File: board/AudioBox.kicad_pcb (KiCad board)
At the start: 2 copper layers, 81.6 x 85 mm, 92 parts, among them J1 Conn_01x04_Male, J2 Conn_Coaxial_Power, J3 AudioJack3_SwitchT, J4 Conn_02x20_Odd_Even, U1 AD1938, U10 LDLN030, U2 TS912, U3 TS912, U4 TS912, U5 TS912, Y1 12.288 MHz

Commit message: half placement done
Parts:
- removed J1: Conn_01x04_Male, Connector_PinHeader_2.54mm:PinHeader_1x04_P2.54mm_Vertical
- removed J2: Conn_Coaxial_Power, Connector_BarrelJack:BarrelJack_Wuerth_6941xx301002
- removed R7: 100K, Resistor_SMD:R_0603_1608Metric_Pad1.05x0.95mm_HandSolder
- C1, C10, C2, C28, C3, C30, C31, C32, C34, C35, C36, C37, C39, C4, C40, C5, C6, C7, C8, C9, R19, R20, R22, R23, R24, R25, R28, R29, R32, R33, U5: moved to B.Cu
- C12: value 10u -> 22u
- IN1, IN2, OUT1, OUT2: value 4833.222_SCH -> 4833.222
- R3: value 4.7K -> 2.2K
- moved C35 77.0 mm to (140.1, 65.7)
- moved U5 73.8 mm to (141.1, 62.4)
- moved C36 73.2 mm to (140.8, 65.1)
- moved C34 70.0 mm to (141.4, 73.5)
- moved R23 66.4 mm to (142.6, 63.5)
- moved IN2 61.2 mm to (102.7, 102.0)
- moved R25 59.4 mm to (143.0, 68.5)
- moved C37 58.6 mm to (140.7, 69.8)
- moved R22 53.4 mm to (140.2, 72.6)
- moved U10 51.4 mm to (96.7, 34.0), turned to 270 degrees
- moved R24 50.6 mm to (140.3, 63.4)
- moved R1 47.2 mm to (49.0, 35.9)
- moved R30 46.5 mm to (44.3, 77.8), turned to 180 degrees
- moved C11 45.0 mm to (99.0, 78.7)
- moved R27 43.5 mm to (53.3, 71.7), turned to 270 degrees
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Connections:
- C12 pad 1: IN_1 -> Net-(C12-Pad1)
- C12 pad 2: Net-(C12-Pad2) -> IN_1
- C27 pad 2: +5VA -> +5V
- J4 pad 10: Net-(J4-Pad10) -> (no net)
- J4 pad 11: Net-(J4-Pad11) -> (no net)
- J4 pad 13: Net-(J4-Pad13) -> (no net)
- J4 pad 15: Net-(J4-Pad15) -> (no net)
- J4 pad 16: Net-(J4-Pad16) -> (no net)
- J4 pad 18: Net-(J4-Pad18) -> (no net)
- J4 pad 22: Net-(J4-Pad22) -> (no net)
- J4 pad 26: Net-(J4-Pad26) -> (no net)
- J4 pad 27: Net-(J4-Pad27) -> (no net)
- J4 pad 28: Net-(J4-Pad28) -> (no net)
- J4 pad 29: Net-(J4-Pad29) -> (no net)
- J4 pad 3: Net-(J4-Pad3) -> (no net)
- J4 pad 31: Net-(J4-Pad31) -> (no net)
- J4 pad 33: Net-(J4-Pad33) -> (no net)
- J4 pad 36: Net-(J4-Pad36) -> (no net)
- J4 pad 37: Net-(J4-Pad37) -> (no net)
- J4 pad 5: Net-(J4-Pad5) -> (no net)
- J4 pad 7: Net-(J4-Pad7) -> (no net)
- J4 pad 8: Net-(J4-Pad8) -> (no net)
- R3 pad 2: ADC_CM -> Net-(C12-Pad1)
- U1 pad 11: Net-(U1-Pad11) -> (no net)
- U1 pad 14: Net-(U1-Pad14) -> (no net)
- U1 pad 15: Net-(U1-Pad15) -> (no net)
- U1 pad 19: Net-(U1-Pad19) -> (no net)
- U1 pad 43: Net-(U1-Pad43) -> (no net)
- U1 pad 44: Net-(U1-Pad44) -> (no net)
- U1 pad 45: Net-(U1-Pad45) -> (no net)
- U1 pad 46: Net-(U1-Pad46) -> (no net)
- U1 pad 6: Net-(U1-Pad6) -> (no net)
- U1 pad 7: Net-(U1-Pad7) -> (no net)
- U1 pad 8: Net-(U1-Pad8) -> (no net)
- U1 pad 9: Net-(U1-Pad9) -> (no net)
- U10 pad 1: +5VA -> +5V
- U10 pad 3: +5VA -> +5V
- U3 pad 1: Net-(C20-Pad1) -> Net-(C19-Pad2)
- U3 pad 2: Net-(R3-Pad1) -> Net-(R10-Pad1)
- U3 pad 3: Net-(C12-Pad2) -> ADC_CM
- U3 pad 6: Net-(R10-Pad1) -> Net-(R3-Pad1)
- U3 pad 7: Net-(C19-Pad2) -> Net-(C20-Pad1)
- U4 pad 1: Net-(C22-Pad1) -> Net-(C21-Pad1)
- U4 pad 2: Net-(R4-Pad1) -> Net-(R11-Pad1)
- U4 pad 6: Net-(R11-Pad1) -> Net-(R4-Pad1)
- U4 pad 7: Net-(C21-Pad1) -> Net-(C22-Pad1)

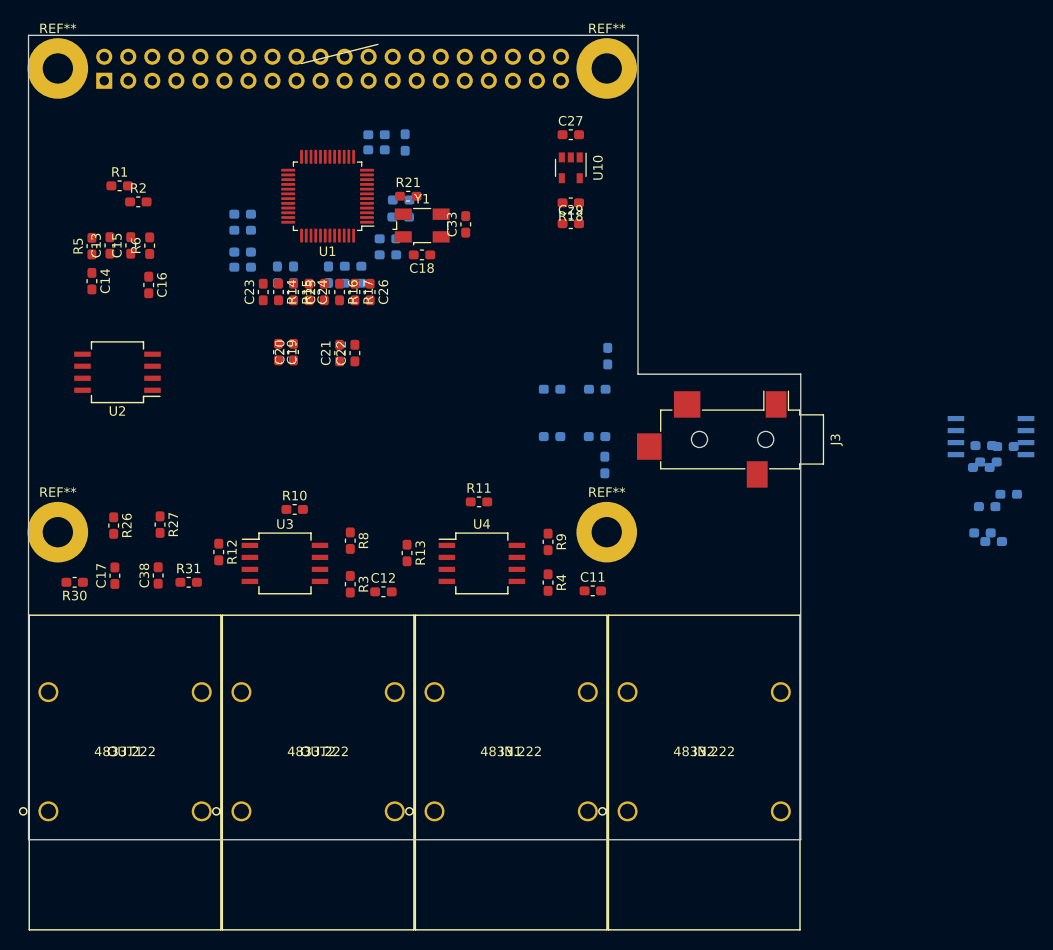
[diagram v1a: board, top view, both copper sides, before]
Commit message: finished routing. Silkskreen to do
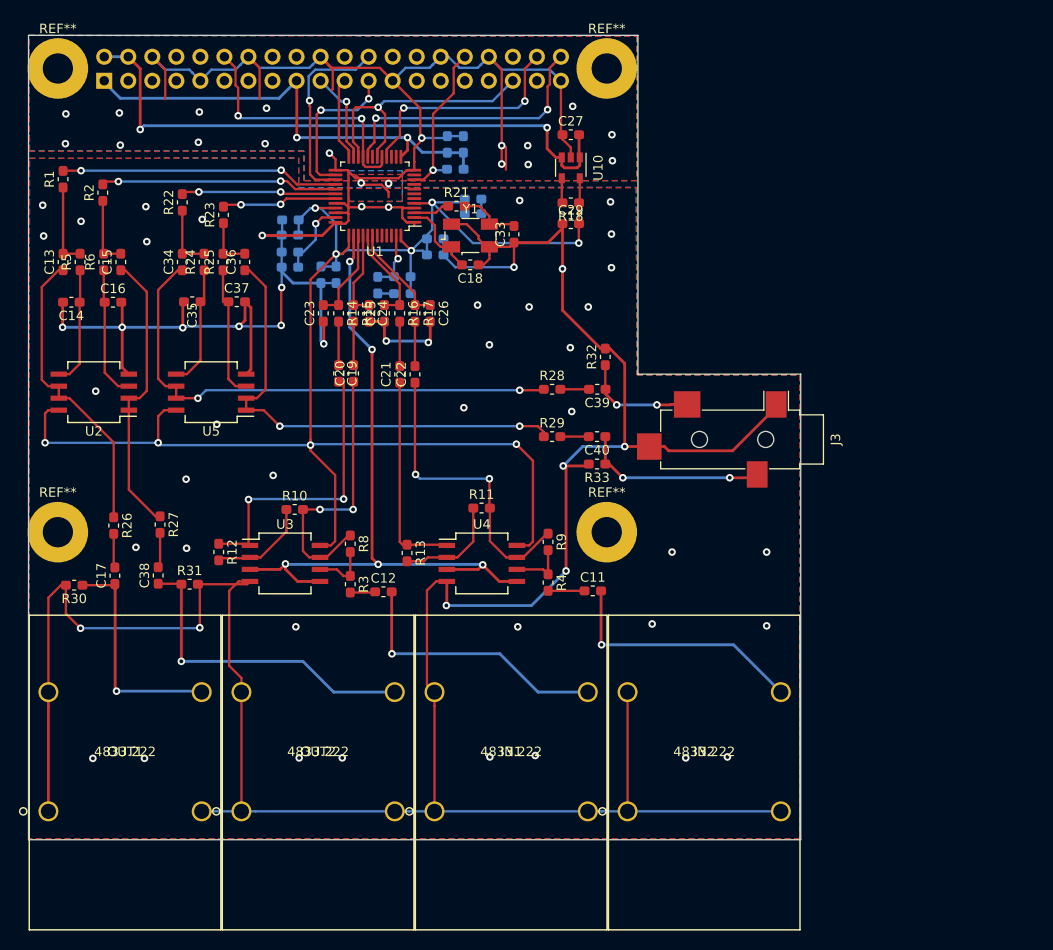
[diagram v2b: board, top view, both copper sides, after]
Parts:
- C34, C35, C36, C37, C39, C40, R22, R23, R24, R25, R28, R29, R32, R33, U5: moved to F.Cu
- moved R22 91.5 mm to (55.6, 37.6), turned to 90 degrees
- moved C34 90.7 mm to (55.6, 44.0), turned to 90 degrees
- moved R25 86.6 mm to (60.0, 44.0), turned to 90 degrees
- moved R23 86.2 mm to (60.0, 39.0), turned to 90 degrees
- moved C35 85.2 mm to (56.7, 48.1), turned to 180 degrees
- moved R24 84.6 mm to (58.0, 44.0), turned to 90 degrees
- moved U5 82.5 mm to (58.7, 57.7), turned to 180 degrees
- moved C37 82.2 mm to (61.4, 48.1)
- moved C36 81.4 mm to (62.2, 44.0), turned to 90 degrees
- moved C2 9.19 mm to (85.3, 31.5), turned to 270 degrees
- moved C8 7.66 mm to (86.4, 38.9)
- moved C7 7.60 mm to (86.4, 37.3)
- moved C1 7.54 mm to (83.7, 31.5), turned to 270 degrees
- moved C19 6.74 mm to (72.2, 55.7)
- moved C21 6.74 mm to (78.6, 55.8)
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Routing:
- net GND: track 0.00 -> 527.5 mm, vias 0 -> 76
- net VDDA: track 0.00 -> 180.4 mm, vias 0 -> 9
- net ADC_CM: track 0.00 -> 74.1 mm, vias 0 -> 5
- net +5V: track 0.00 -> 64.4 mm, vias 0 -> 2
- net Net-(C34-Pad1): track 0.00 -> 55.5 mm, vias 0 -> 2
- net Net-(C36-Pad1): track 0.00 -> 50.4 mm, vias 0 -> 2
- net +3V3: track 0.00 -> 50.3 mm, vias 0 -> 2
- net OUT_2: track 0.00 -> 34.5 mm, vias 0 -> 1
- net Net-(C22-Pad1): track 0.00 -> 32.2 mm, vias 0 -> 2
- net Net-(C13-Pad1): track 0.00 -> 31.8 mm
- net Net-(C19-Pad2): track 0.00 -> 31.2 mm, vias 0 -> 2
- net Net-(C15-Pad1): track 0.00 -> 30.5 mm
- net Net-(C20-Pad1): track 0.00 -> 29.4 mm, vias 0 -> 2
- net OL_1: track 0.00 -> 29.4 mm, vias 0 -> 2
- net /SAI_FSA: track 0.00 -> 29.2 mm, vias 0 -> 1
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- added copper zone on B.Cu, net GND
- added copper zone on F.Cu, net GND

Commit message: updated silkscreen
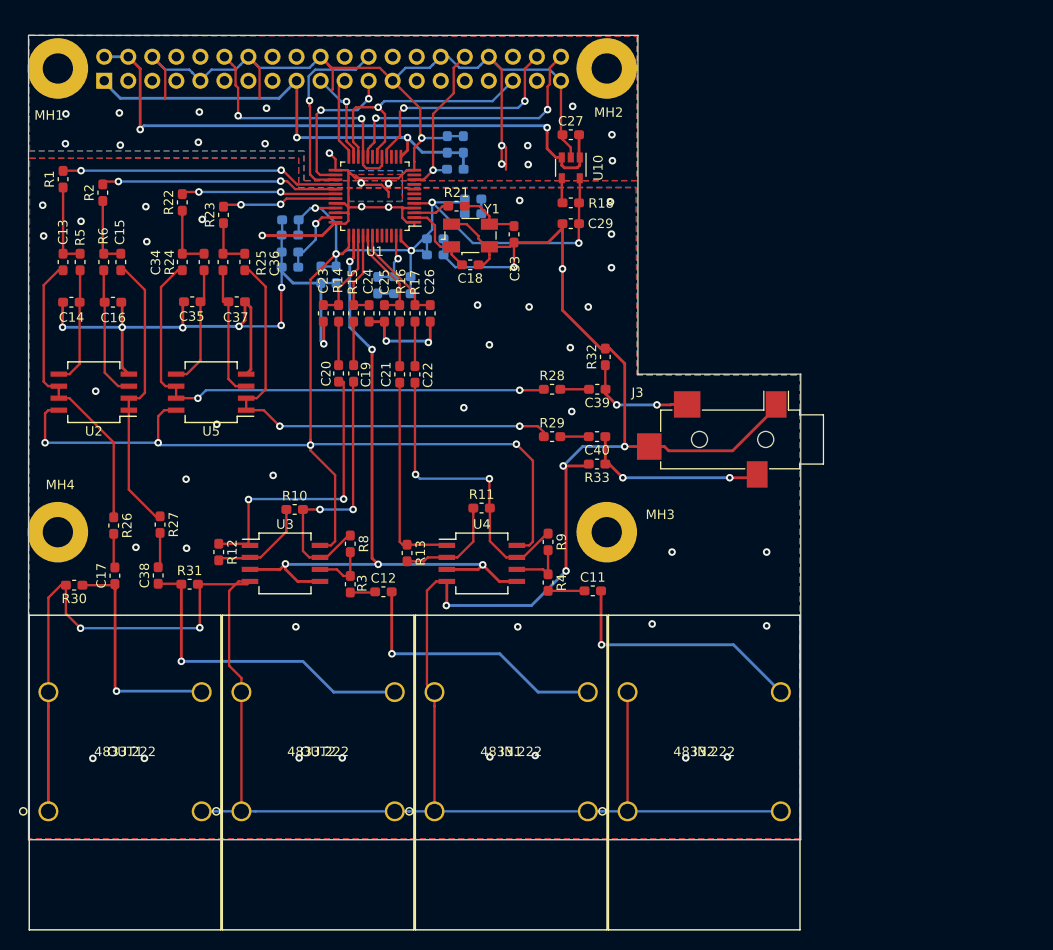
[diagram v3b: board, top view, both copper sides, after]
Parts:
- renumbered REF** to MH1, REF** to MH2, REF** to MH3, REF** to MH4
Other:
- board text added: "STM32MP1 Audio Box v1.0"

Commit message: minor and generate Gerber
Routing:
- net ADC_CM: track 74.1 -> 73.4 mm
- net GND: vias 76 -> 78
